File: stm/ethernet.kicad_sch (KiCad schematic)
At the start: 4 parts, among them U3 LAN8742A, Y1 25M

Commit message: ethernet phy
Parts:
- added C33, C34: C, symbol Device:C
- added C35: 470p, symbol Device:C
- added C36, C37, C38: 1u, symbol Device:C
- added D1, D2, D3: LED, symbol Device:LED
- added J4: ARJM11A1-009-AB-EW2, ARJM11A1-009-AB-EW2_ABR, symbol ARJM11A1-009-AB-EW2:ARJM11A1-009-AB-EW2
- added R12: 12.1k, symbol Device:R
- added R13: 270, symbol Device:R
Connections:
- net GND: now also U3.25 (VSS), C33.2, C34.2, C35.2, C36.2, C37.2, C38.2, J4.8 (GND), R12.2, R13.2
- net +3.3V: now reaches U3.1 (VDD2A)
- net +3.3V: now also U3.19 (VDD1A), U3.9 (VDDIO), C33.1, C34.1, C37.1, C38.1
- net ETH_CRS_DV: now reaches U3.11 (CRS_DV/MODE2)
- net ETH_MDIO: now reaches U3.12 (MDIO)
- net ETH_MDC: now reaches U3.13 (MDC)
- net ETH_REF_CLK: now reaches U3.14 (~{INT}/REFCLKO)
- net ETH_TX_EN: now reaches U3.16 (TXEN)
- net ETH_TXD0: now reaches U3.17 (TXD0)
- net ETH_TXD1: now reaches U3.18 (TXD1)
- net ETH_TXD_N: now reaches U3.20 (TXN)
- net ETH_TXD_N: now also J4.2 (TD-)
- net ETH_TXD_P: now reaches U3.21 (TXP)
- net ETH_TXD_P: now also J4.1 (TD+)
- net ETH_RXD_N: now reaches U3.22 (RXN)
- net ETH_RXD_N: now also J4.6 (RD-)
- net ETH_RXD_P: now reaches U3.23 (RXP)
- net ETH_RXD_P: now also J4.3 (RD+)
- net at U3.24 (RBIAS): now also R12.1
- net at U3.3 (LED1/REGOFF): now also D3.2 (A)
- net VDDCR: now reaches U3.6 (VDDCR)
- net VDDCR: now also C35.1, C36.1
- net ETH_RXD1: now reaches U3.7 (RXD1/MODE1)
- net ETH_RXD0: now reaches U3.8 (RXD0/MODE0)
- new net: D3.1 (K), R13.1
- new net: D2.1 (K), J4.12 (CATHODE)
- new net: D2.2 (A), J4.11 (ANODE)
- new net: D1.1 (K), J4.10 (CATHODE)
- new net: D1.2 (A), J4.9 (ANODE)
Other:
- moved on the sheet: C28, C29, U3, Y1

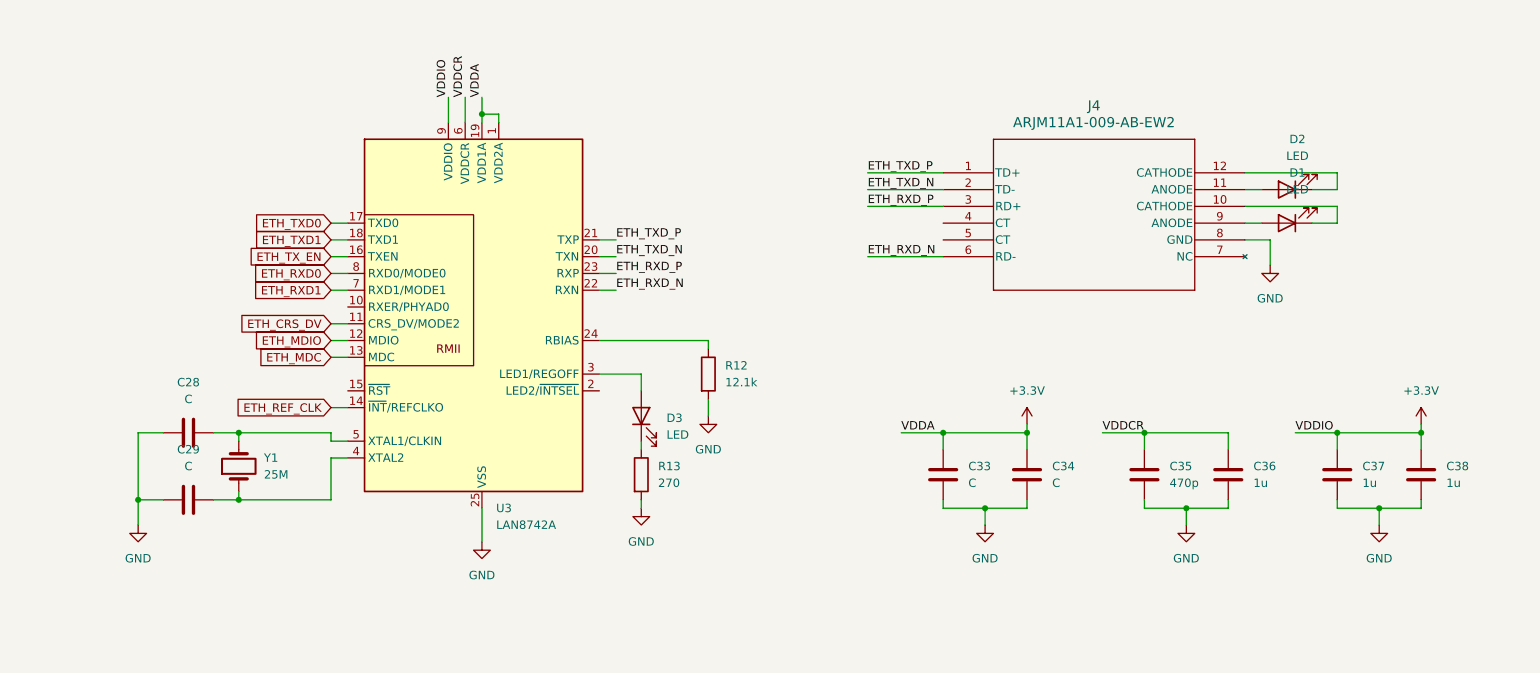
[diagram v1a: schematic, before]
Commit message: regoff/intsel pins
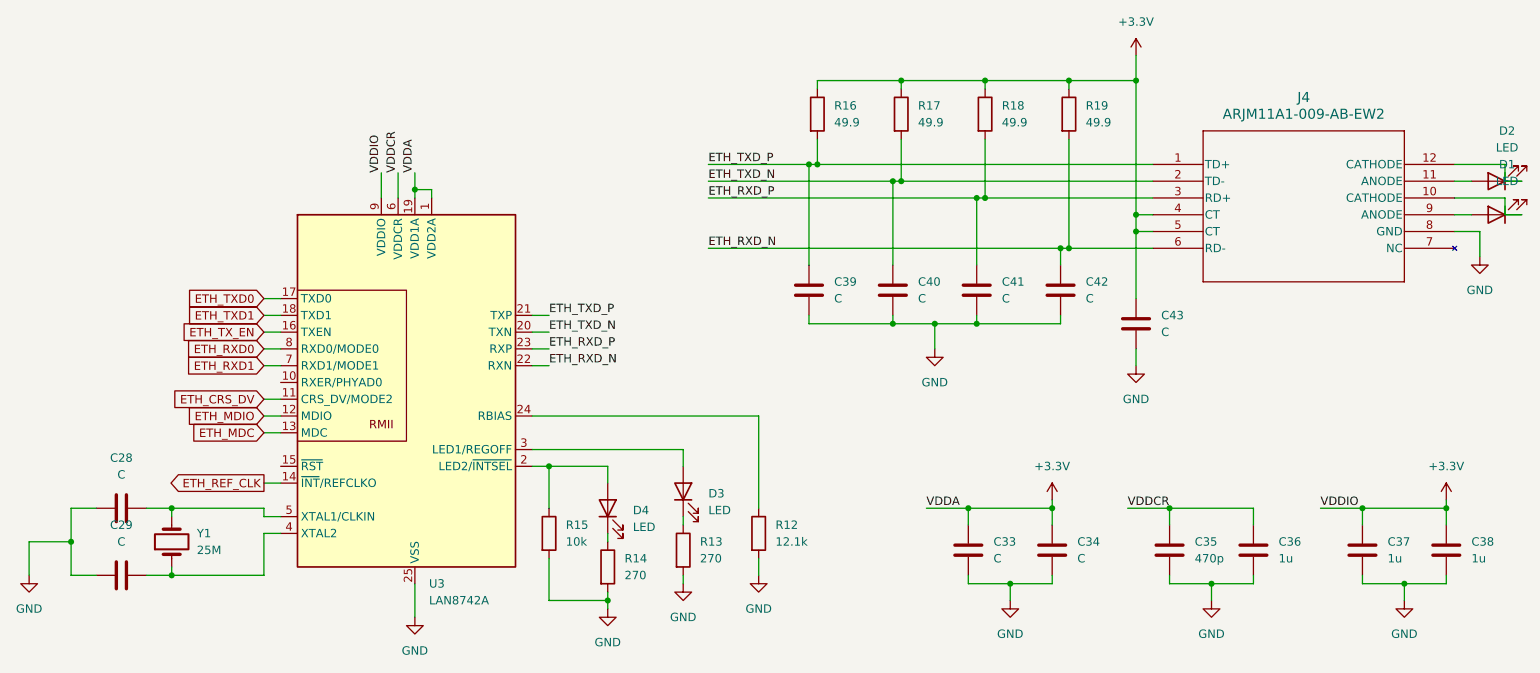
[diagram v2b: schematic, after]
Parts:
- added C39, C40, C41, C42, C43: C, symbol Device:C
- added D4: LED, symbol Device:LED
- added R14: 270, symbol Device:R
- added R15: 10k, symbol Device:R
- added R16, R17, R18, R19: 49.9, symbol Device:R
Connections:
- net +3.3V: now also J4.4 (CT), J4.5 (CT), C43.1, R16.1, R17.1, R18.1, R19.1
- net ETH_RXD_N: now also C42.1, R19.2
- net ETH_RXD_P: now also C41.1, R18.2
- net ETH_TXD_N: now also C40.1, R17.2
- net ETH_TXD_P: now also C39.1, R16.2
- net GND: now also C39.2, C40.2, C41.2, C42.2, C43.2, R14.2, R15.2
- net at U3.2 (LED2/~{INTSEL}): now also D4.2 (A), R15.1
- new net: D4.1 (K), R14.1
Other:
- moved on the sheet: C28, C29, C33, C34, C35, C36, C37, C38, D1, D2, D3, J4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
